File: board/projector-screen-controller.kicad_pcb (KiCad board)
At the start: 2 copper layers, 97.2 x 106 mm, 57 parts, among them J1 ICSP, J2 MSTBVA-3-G, J3 MCV-3-G, J4 MCV-3-G, J5 MCV-3-G, J6 MSTBVA-6-G, J7 MCV-3-G, K1 JS1-12V-F, K2 JS1-12V-F, K3 JS1-12V-F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

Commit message: Bump revision to 0.2
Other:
- board text added: "Motorized Projector Screen Controller Rev 0.2"
- board text removed: "Motorized Projector Screen Controller Rev 0.1"
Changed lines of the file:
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@@
   (title_block
     (title "Projector Screen Controller")
-    (rev 0.1)
+    (date 2019-09-02)
+    (rev 0.2)
     (company "Flirble Open Source")
     (comment 1 https://github.com/flirbleoss/projector-screen-controller)
@@
     (visible_elements 7FFFFF7F)
     (pcbplotparams
-      (layerselection 0x010fc_ffffffff)
+      (layerselection 0x010f0_ffffffff)
       (usegerberextensions false)
       (usegerberattributes false)
@@
       (viasonmask false)
       (mode 1)
-      (useauxorigin false)
+      (useauxorigin true)
       (hpglpennumber 1)
       (hpglpenspeed 20)
@@
       (outputformat 1)
       (mirror false)
-      (drillshape 1)
+      (drillshape 0)
       (scaleselection 1)
-      (outputdirectory ""))
+      (outputdirectory "gerbers/"))
   )
   (net 0 "")
@@
     (effects (font (size 1.2 1.2) (thickness 0.2)))
   )
-  (gr_text "Motorized Projector\nScreen Controller\nRev 0.1" (at 97.79 49.53) (layer F.SilkS)
+  (gr_text "Motorized Projector\nScreen Controller\nRev 0.2" (at 97.79 49.53) (layer F.SilkS)
     (effects (font (size 1.5 1.5) (thickness 0.2)))
   )

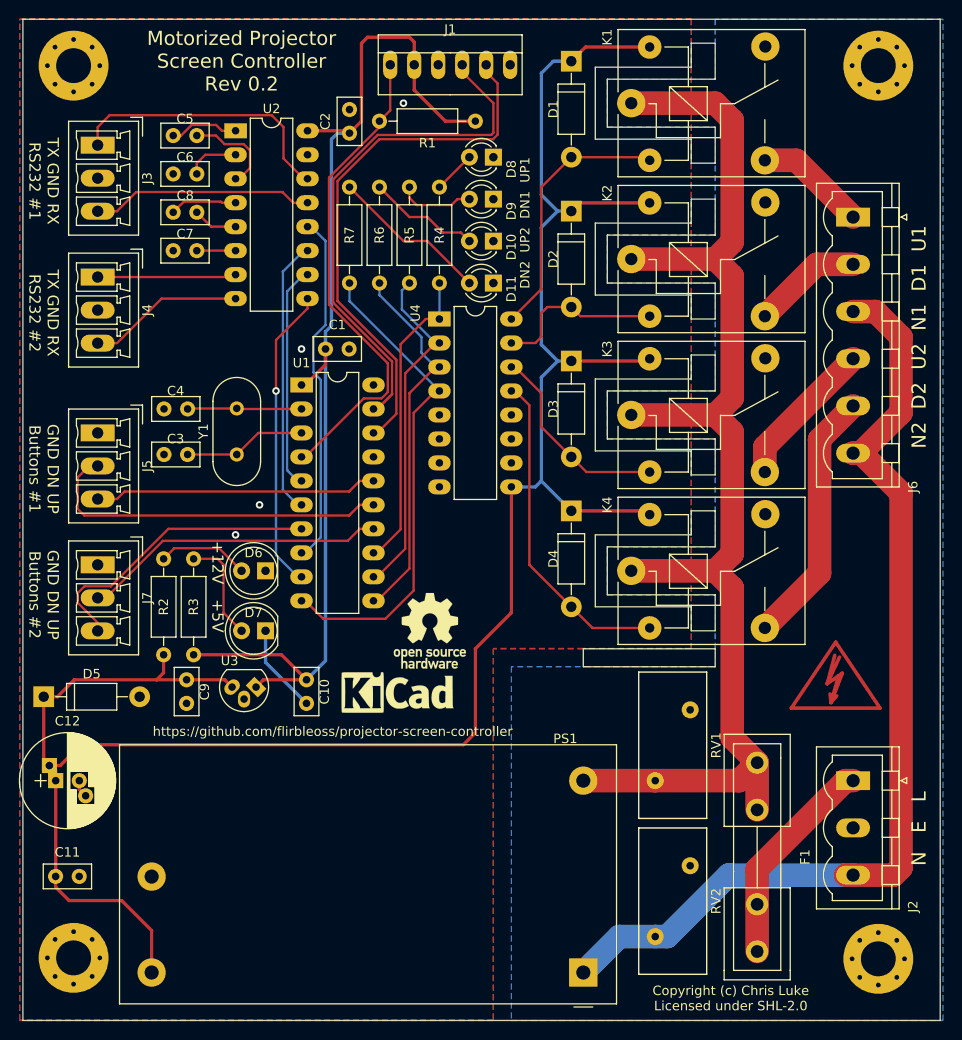
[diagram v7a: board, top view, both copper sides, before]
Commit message: Minor layout tweaks, component updates
* Add an MCU driven status LED
* Update LED current limit resistor values
* Minor trace tweaks for clearance
* Based on empirical measurements of rev 0.1 board, adjust the location of the
  board mounting holes.
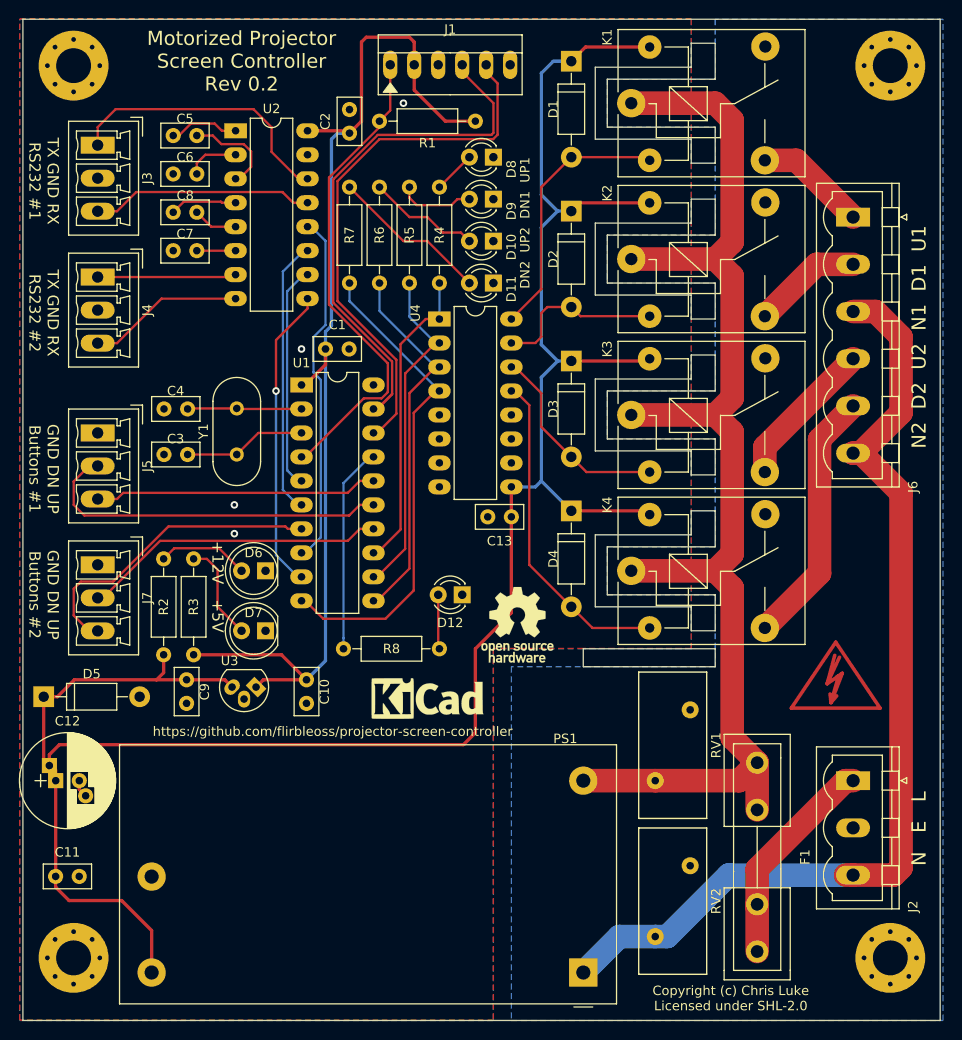
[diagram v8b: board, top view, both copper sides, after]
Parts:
- removed the REF** at (165.2, 144.6)
- removed the REF** at (165.2, 50.0)
- added C13: 0.1uF, Capacitors_THT:C_Disc_D5.0mm_W2.5mm_P2.50mm, F.Cu at (126.4, 97.8)
- added D12: LED, LEDs:LED_D3.0mm, F.Cu at (121.2, 106.0)
- added R8: 330R, Resistors_THT:R_Axial_DIN0207_L6.3mm_D2.5mm_P10.16mm_Horizontal, F.Cu at (108.6, 111.8)
- added REF**: MountingHole_3.7mm_Pad_Via, Mounting_Holes:MountingHole_3.7mm_Pad_Via, F.Cu at (166.5, 144.5)
- added REF**: MountingHole_3.7mm_Pad_Via, Mounting_Holes:MountingHole_3.7mm_Pad_Via, F.Cu at (166.5, 50.0)
- R2: value 500R -> 1K
- R3, R4, R5, R6, R7: value 150R -> 330R
- moved REF*** 9.29 mm to (127.0, 109.2)
- moved REF** 3.24 mm to (117.5, 116.8)
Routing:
- net Net-(R8-Pad1): track 0.00 -> 21.9 mm
- net GND: track 13.2 -> 3.68 mm
- net Net-(D12-Pad2): track 0.00 -> 5.77 mm
- net Net-(D7-Pad2): track 11.2 -> 10.5 mm
- net /MCU/D1_DN_TTL: track 37.1 -> 36.4 mm
- net +12V: track 230.0 -> 230.7 mm
